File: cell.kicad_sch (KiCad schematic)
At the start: 5 parts, among them Q7 BSS84

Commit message: update
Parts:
- added D9: RED, LED_SMD:LED_0805_2012Metric, symbol Device:LED
- added R47: 470, Resistor_SMD:R_0805_2012Metric, symbol Device:R
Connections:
- net CELL-: now also R47.1
- net at Q7.3 (D), R21.2: now also D9.2 (A)
- new net: D9.1 (K), R47.2
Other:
- moved on the sheet: R21
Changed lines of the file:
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@@
   (junction (at 134.62 68.58) (diameter 0) (color 0 0 0 0)
   )
+  (junction (at 149.86 83.82) (diameter 0) (color 0 0 0 0)
+  )
   (junction (at 110.49 68.58) (diameter 0) (color 0 0 0 0)
+  )
+  (junction (at 134.62 83.82) (diameter 0) (color 0 0 0 0)
+  )
+  (wire (pts (xy 134.62 93.98) (xy 134.62 96.52))
+    (stroke (width 0) (type default) (color 0 0 0 0))
   )
   (wire (pts (xy 152.4 68.58) (xy 134.62 68.58))
@@
     (stroke (width 0) (type default) (color 0 0 0 0))
   )
-  (wire (pts (xy 134.62 81.28) (xy 139.7 81.28))
+  (wire (pts (xy 134.62 83.82) (xy 134.62 86.36))
+    (stroke (width 0) (type default) (color 0 0 0 0))
+  )
+  (wire (pts (xy 149.86 96.52) (xy 149.86 83.82))
     (stroke (width 0) (type default) (color 0 0 0 0))
   )
@@
     (stroke (width 0) (type default) (color 0 0 0 0))
   )
-  (wire (pts (xy 147.32 81.28) (xy 152.4 81.28))
+  (wire (pts (xy 147.32 83.82) (xy 149.86 83.82))
     (stroke (width 0) (type default) (color 0 0 0 0))
   )
@@
     (stroke (width 0) (type default) (color 0 0 0 0))
   )
+  (wire (pts (xy 147.32 96.52) (xy 149.86 96.52))
+    (stroke (width 0) (type default) (color 0 0 0 0))
+  )
   (wire (pts (xy 123.19 76.2) (xy 127 76.2))
+    (stroke (width 0) (type default) (color 0 0 0 0))
+  )
+  (wire (pts (xy 134.62 81.28) (xy 134.62 83.82))
     (stroke (width 0) (type default) (color 0 0 0 0))
   )
@@
     (stroke (width 0) (type default) (color 0 0 0 0))
   )
+  (wire (pts (xy 139.7 96.52) (xy 134.62 96.52))
+    (stroke (width 0) (type default) (color 0 0 0 0))
+  )
   (wire (pts (xy 110.49 68.58) (xy 120.65 68.58))
     (stroke (width 0) (type default) (color 0 0 0 0))
   )
+  (wire (pts (xy 149.86 83.82) (xy 152.4 83.82))
+    (stroke (width 0) (type default) (color 0 0 0 0))
+  )
   (wire (pts (xy 90.17 68.58) (xy 110.49 68.58))
+    (stroke (width 0) (type default) (color 0 0 0 0))
+  )
+  (wire (pts (xy 134.62 83.82) (xy 139.7 83.82))
     (stroke (width 0) (type default) (color 0 0 0 0))
   )
@@
     (effects (font (size 1.27 1.27)) (justify right))
   )
-  (hierarchical_label "CELL-" (shape input) (at 152.4 81.28 0)
+  (hierarchical_label "CELL-" (shape input) (at 152.4 83.82 0)
     (effects (font (size 1.27 1.27)) (justify left))
   )
@@
     (pin "2")
   )
-  (symbol (lib_id "Device:R") (at 143.51 81.28 270) (unit 1)
+  (symbol (lib_id "Device:R") (at 143.51 83.82 270) (unit 1)
     (in_bom yes) (on_board yes)
-    (property "Reference" "R21" (id 0) (at 143.51 85.09 90))
-    (property "Value" "33" (id 1) (at 143.51 87.63 90))
-    (property "Footprint" "Resistor_SMD:R_2512_6332Metric" (id 2) (at 143.51 79.502 90)
+    (property "Reference" "R21" (id 0) (at 143.51 87.63 90))
+    (property "Value" "33" (id 1) (at 143.51 90.17 90))
+    (property "Footprint" "Resistor_SMD:R_2512_6332Metric" (id 2) (at 143.51 82.042 90)
       (effects (font (size 1.27 1.27)) hide)
     )
-    (property "Datasheet" "~" (id 3) (at 143.51 81.28 0)
+    (property "Datasheet" "~" (id 3) (at 143.51 83.82 0)
       (effects (font (size 1.27 1.27)) hide)
     )
@@
       (effects (font (size 1.27 1.27)) hide)
     )
+    (pin "1")
+    (pin "2")
+  )
+  (symbol (lib_id "Device:R") (at 143.51 96.52 270) (unit 1)
+    (in_bom yes) (on_board yes)
+    (property "Reference" "R47" (id 0) (at 143.51 100.33 90))
+    (property "Value" "470" (id 1) (at 143.51 102.87 90))
+    (property "Footprint" "Resistor_SMD:R_0805_2012Metric" (id 2) (at 143.51 94.742 90)
+      (effects (font (size 1.27 1.27)) hide)
+    )
+    (property "Datasheet" "~" (id 3) (at 143.51 96.52 0)
+      (effects (font (size 1.27 1.27)) hide)
+    )
+    (pin "1")
+    (pin "2")
+  )
+  (symbol (lib_id "Device:LED") (at 134.62 90.17 90) (unit 1)
+    (in_bom yes) (on_board yes) (fields_autoplaced)
+    (property "Reference" "D9" (id 0) (at 138.43 90.4874 90)
+      (effects (font (size 1.27 1.27)) (justify right))
+    )
+    (property "Value" "RED" (id 1) (at 138.43 93.0274 90)
+      (effects (font (size 1.27 1.27)) (justify right))
+    )
+    (property "Footprint" "LED_SMD:LED_0805_2012Metric" (id 2) (at 134.62 90.17 0)
+      (effects (font (size 1.27 1.27)) hide)
+    )
+    (property "Datasheet" "~" (id 3) (at 134.62 90.17 0)
+      (effects (font (size 1.27 1.27)) hide)
+    )

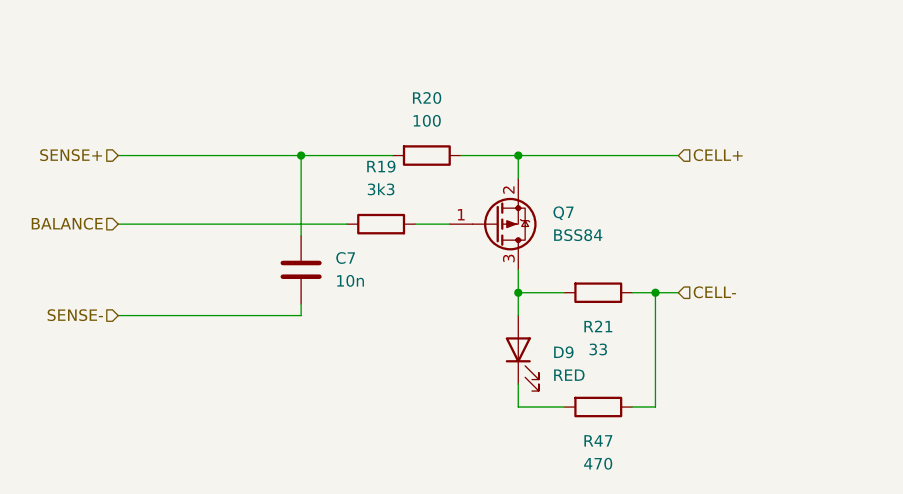
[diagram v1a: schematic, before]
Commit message: new board dimensions
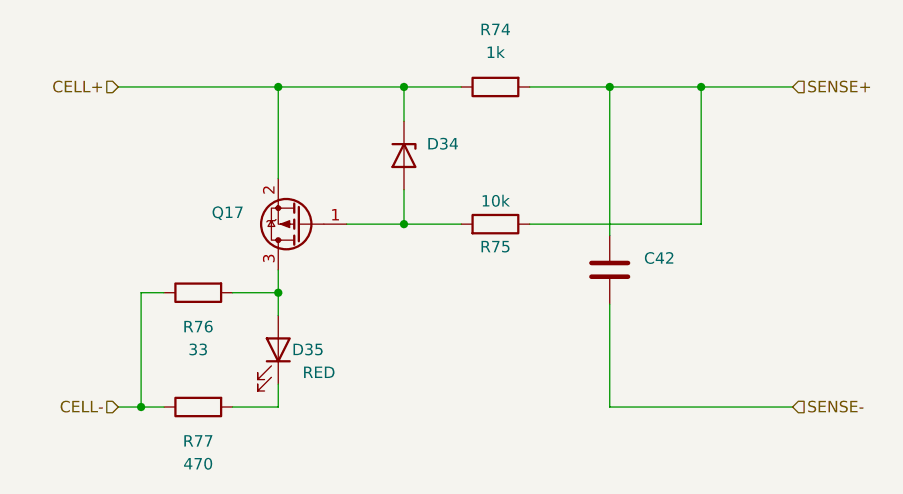
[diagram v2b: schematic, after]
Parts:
- removed C7: 10n, Capacitor_SMD:C_0805_2012Metric, symbol Device:C
- removed D9: RED, LED_SMD:LED_0805_2012Metric, symbol Device:LED
- removed Q7: BSS84, Package_TO_SOT_SMD:SOT-23, symbol Transistor_FET:BSS84
- removed R19: 3k3, Resistor_SMD:R_0805_2012Metric, symbol Device:R
- removed R20: 100, Resistor_SMD:R_0805_2012Metric, symbol Device:R
- removed R21: 33, Resistor_SMD:R_2512_6332Metric, symbol Device:R
- removed R47: 470, Resistor_SMD:R_0805_2012Metric, symbol Device:R
- added C42: ~, Capacitor_SMD:C_0805_2012Metric, symbol Device:C
- added D34: ~, Diode_SMD:D_SOD-323, symbol Device:D_Zener
- added D35: RED, LED_SMD:LED_0805_2012Metric, symbol Device:LED
- added Q17: ~, Package_TO_SOT_SMD:SOT-23, symbol Transistor_FET:BSS84
- added R74: 1k, Resistor_SMD:R_0805_2012Metric, symbol Device:R
- added R75: 10k, Resistor_SMD:R_0805_2012Metric, symbol Device:R
- added R76: 33, Resistor_SMD:R_2512_6332Metric, symbol Device:R
- added R77: 470, Resistor_SMD:R_0805_2012Metric, symbol Device:R
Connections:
- net CELL+: now also D34.1 (K), Q17.2 (S), R74.1
- net CELL-: now also R76.1, R77.1
- net SENSE+: now also C42.1, R74.2, R75.1
- net SENSE-: now also C42.2
- new net: D35.1 (K), R77.2
- new net: D35.2 (A), Q17.3 (D), R76.2
- new net: D34.2 (A), Q17.1 (G), R75.2

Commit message: almost ready to order
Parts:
- C42: value ~ -> 220n; LCSC C52923 -> (none)
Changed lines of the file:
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@@
       (effects (font (size 1.27 1.27)) (justify right))
     )
-    (property "Value" "~" (id 1) (at 148.59 82.5499 0)
+    (property "Value" "220n" (id 1) (at 148.59 82.5499 0)
       (effects (font (size 1.27 1.27)) (justify right))
     )
@@
       (effects (font (size 1.27 1.27)) hide)
     )
-    (property "LCSC" " C52923" (id 5) (at 144.78 81.28 0)
+    (property "LCSC" "" (id 5) (at 144.78 81.28 0)
       (effects (font (size 1.27 1.27)) hide)
     )

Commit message: before switching to kicad 7
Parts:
- C42: LCSC (none) -> C107131
- R74: LCSC (none) -> C17513
- R75: LCSC (none) -> C17414
- R76: LCSC (none) -> C2934070
- R77: LCSC (none) -> C17710
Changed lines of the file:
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@@
       (effects (font (size 1.27 1.27)) hide)
     )
-    (property "LCSC" "" (id 5) (at 144.78 81.28 0)
+    (property "LCSC" "C107131" (id 5) (at 144.78 81.28 0)
       (effects (font (size 1.27 1.27)) hide)
     )
@@
       (effects (font (size 1.27 1.27)) hide)
     )
-    (property "LCSC" "" (id 4) (at 132.08 76.2 90)
+    (property "LCSC" "C17414" (id 4) (at 132.08 76.2 90)
       (effects (font (size 1.27 1.27)) hide)
     )
@@
       (effects (font (size 1.27 1.27)) hide)
     )
-    (property "LCSC" "" (id 4) (at 132.08 60.96 90)
+    (property "LCSC" "C17513" (id 4) (at 132.08 60.96 90)
       (effects (font (size 1.27 1.27)) hide)
     )
@@
       (effects (font (size 1.27 1.27)) hide)
     )
-    (property "LCSC" "" (id 4) (at 99.06 96.52 90)
+    (property "LCSC" "C17710" (id 4) (at 99.06 96.52 90)
       (effects (font (size 1.27 1.27)) hide)
     )
@@
       (effects (font (size 1.27 1.27)) hide)
     )
+    (property "LCSC" "C2934070" (id 4) (at 99.06 83.82 0)
+      (effects (font (size 1.27 1.27)) hide)
+    )

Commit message: V0.2
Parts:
- C42: LCSC C107131 -> C5378
- D34: footprint Diode_SMD:D_SOD-323 -> Diode_SMD:D_SOD-323_HandSoldering
- Q17: LCSC C193020 -> C8492
- R76: value 33 -> 100
